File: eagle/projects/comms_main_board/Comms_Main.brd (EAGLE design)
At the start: 101.6 x 95.2 mm, 202 parts, among them J1101 MOL-SL-3-RA, J1102 MOL-SL-2-RA, J1103 MOL-SL-3-RA, J1104 MOL-SL-3-RA, J1105 MOL-SL-3-RA, J1106 MOL-SL-3-RA, J1107 MOL-SL-5-RA, J1108 MOL-SL-2-RA, J1109 MOL-MINIJR-2P-RA, J1110 MOL-MINIJR-2P-RA, J1111 MOL-SL-3-RA, J1112 MOL-SL-2-RA, J1113 MOL-SL-2-RA, J1114 RECEPTACLE-2x2-254MM, J1115 MOL-MINIJR-2P-RA, J1116 MOL-MINIJR-2P-RA, J1117 RECEPTACLE-2x20-254MM, J701 WRL-00593, J801 PRT-12639, J802 PRT-12639, J803 PRT-12639, J804 PRT-12639, Q501 CSD17579Q3A, U1001 MAX3232CSE+, U1002 MAX4311, U401 LP2985-33DBVR, U402 TPS562209DDCT, U403 MAX6371, U501 2N7002P,215, U502 LM3488MMX/NOPB, U503 NDT2955, U601 TPS562209DDCT, U602 TPS562209DDCT, U603 LP5900SD-3.3/NOPB, U701 MAX-M8Q, U801 MMBT3904-HF, U901 PCT2075D,118, U902 MS560702BA03-50, U903 MCP4541-103E/MS

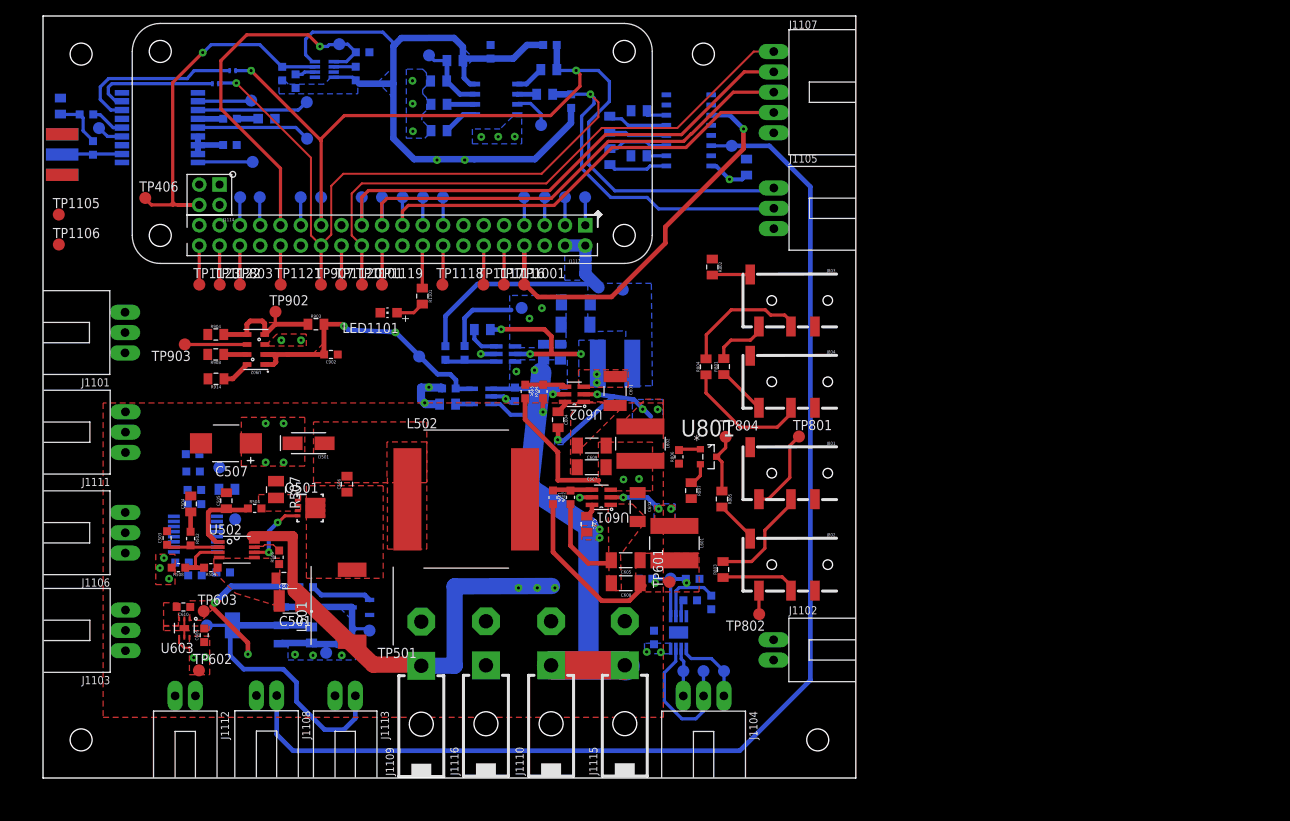
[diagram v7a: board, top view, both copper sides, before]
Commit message: Cleaned up bottom layer, fixed DRCs
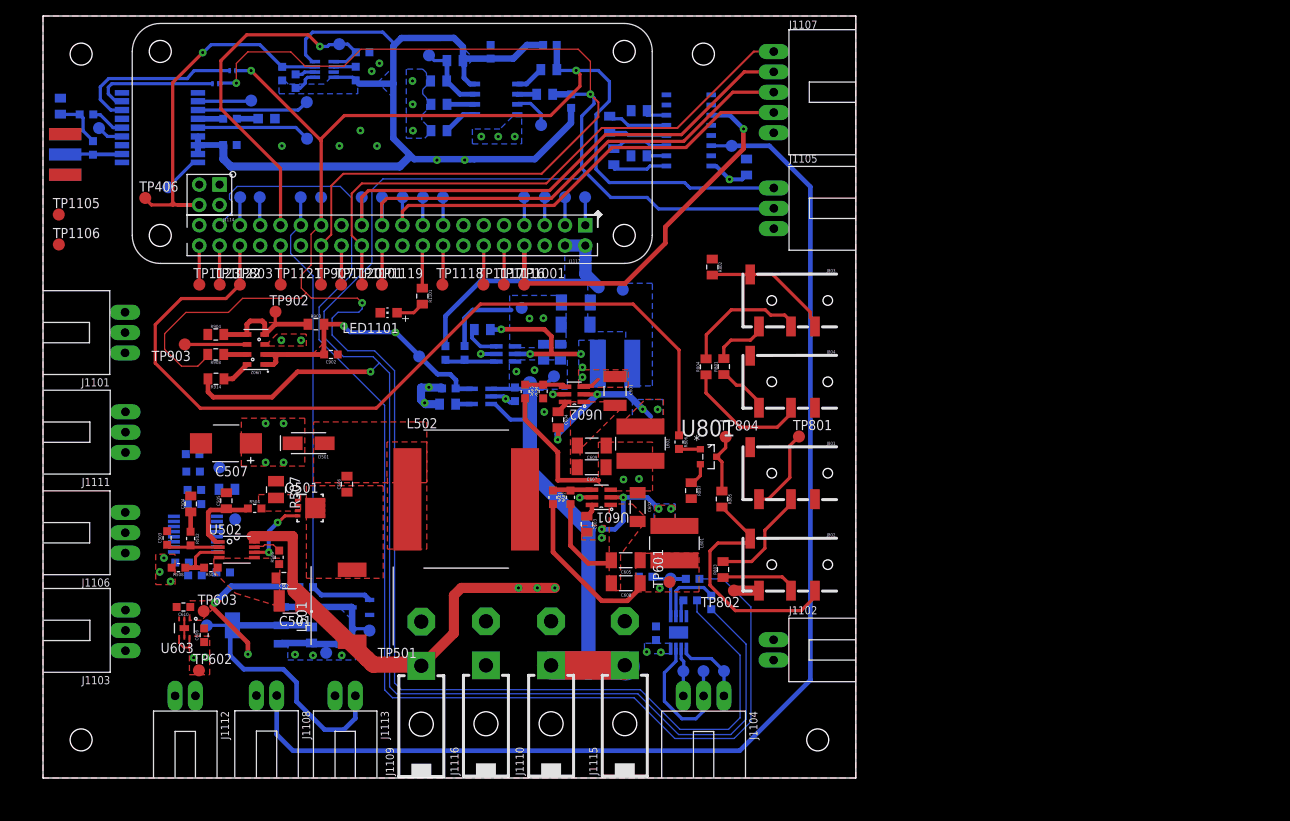
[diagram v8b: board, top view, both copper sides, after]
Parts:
- moved TP702 11.0 mm to (15.7, 73.8)
- moved TP802 4.32 mm to (86.4, 23.4)
- moved R806 1.84 mm to (79.5, 42.0), turned to 270 degrees
- moved TP401 1.66 mm to (63.9, 50.2)
- moved C903 0.59 mm to (76.6, 18.1)
- moved C1003 0.48 mm to (71.3, 77.7)
- moved J701 0.38 mm to (2.77, 75.4)
- moved R915 0.26 mm to (75.3, 25.2)
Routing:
- net SCL: track 121.3 -> 336.4 mm, vias 2 -> 3
- net SDA: track 112.3 -> 276.0 mm, vias 2 -> 3
- net GPIO_POT_HVC: track 0.00 -> 158.9 mm
- net GPIO_PTT: track 4.89 -> 108.6 mm
- net PI_12V_CONTROL: track 11.4 -> 58.3 mm
- net 11P1V_IN: track 59.6 -> 95.1 mm
- net 3P3V_SENSORS: track 130.8 -> 165.4 mm
- net TX_OUT_S: track 5.41 -> 31.3 mm
- net 3P3V_RS232: track 24.7 -> 37.6 mm
- net RX_OUT_S: track 4.76 -> 16.3 mm
- net UART_TXD: track 53.9 -> 47.7 mm
- net BUCK_POT_SW: track 6.61 -> 12.7 mm
- net GPS_ANTENNA: track 7.98 -> 12.0 mm
- net PI_BUCK_SW: track 18.4 -> 21.1 mm
- net 7P4V_IN: track 75.7 -> 73.4 mm
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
